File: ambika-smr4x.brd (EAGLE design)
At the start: 118.7 x 60.3 mm, 100 parts, among them IC1 TL074, IC2 LM13700N, IC3 LM13700N, IC4 LM13700N, IC5 TL072, IC6 MCP4822, IC7 ATMega328p, IC8 4052N, Q1 2N3906, Q2 2N3906, Q3 2N3906, Q4 2N3906, Q5 20MHz, Q6 2N7000, Q7 2N7000

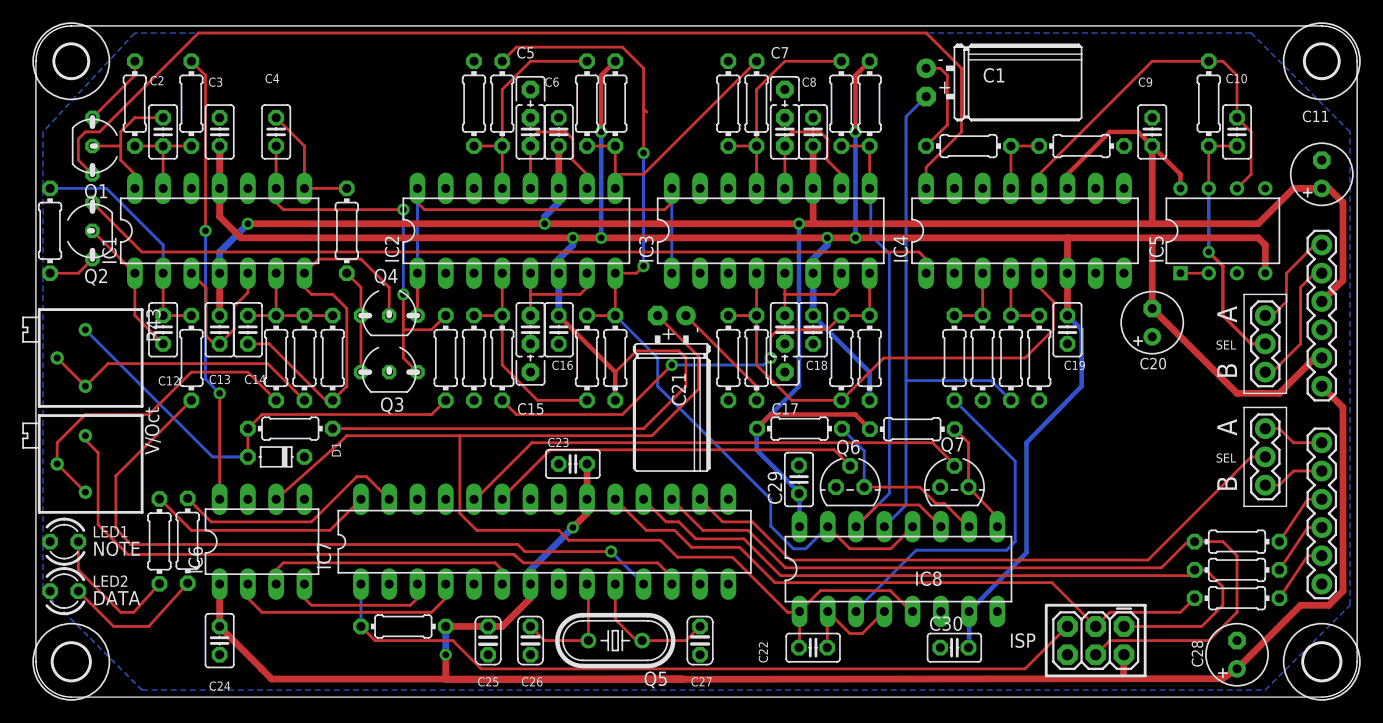
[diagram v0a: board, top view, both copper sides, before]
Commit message: Tidied up board (mainly routing and silkscreen)
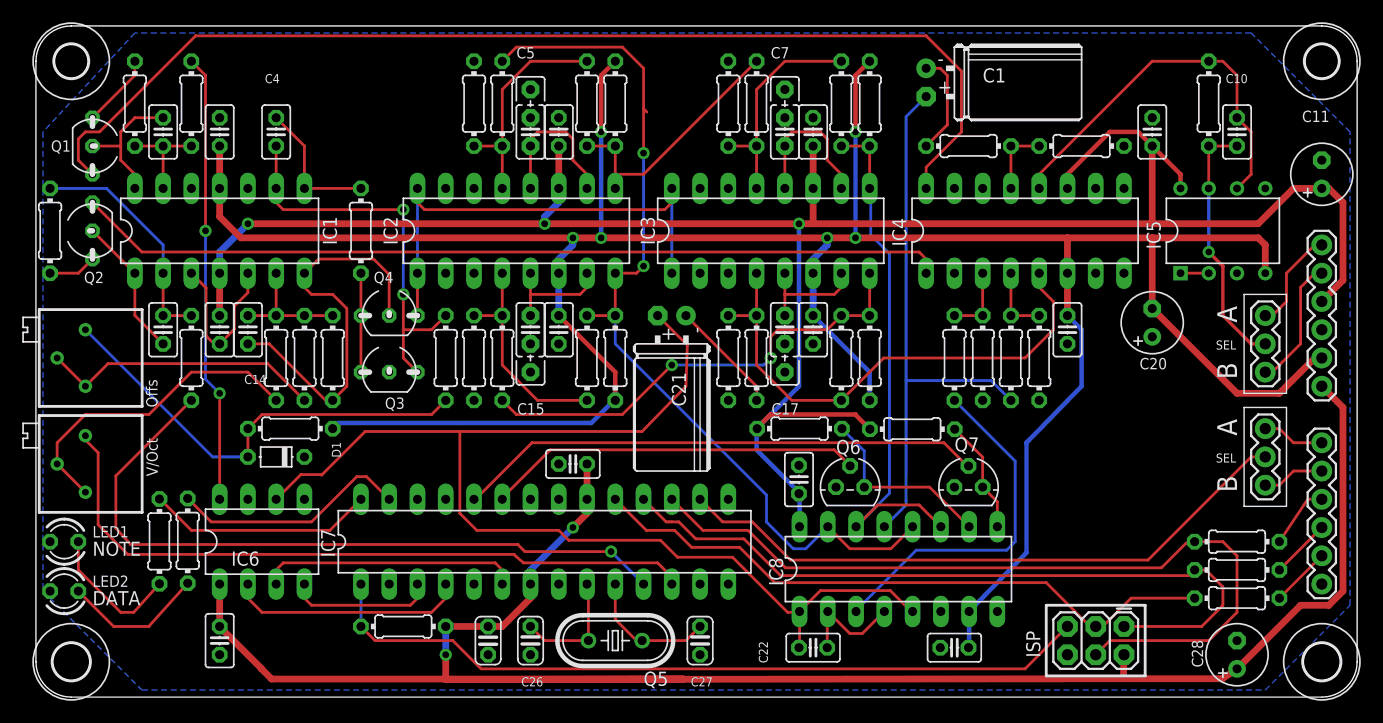
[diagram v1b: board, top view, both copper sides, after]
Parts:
- moved R14 1.27 mm to (29.2, 40.6)
- moved Q7 1.27 mm to (83.8, 17.6)
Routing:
- net VEE: track 282.0 -> 265.2 mm
- net N$9: track 11.2 -> 12.5 mm
- net N$35: track 46.2 -> 47.4 mm
- net OSC: track 106.2 -> 105.2 mm
- net MUXB: track 10.3 -> 11.2 mm
- net N$2: track 36.1 -> 36.8 mm
- net N$1: track 9.42 -> 8.89 mm
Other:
- board text added: "Offs"
